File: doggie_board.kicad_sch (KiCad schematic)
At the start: 1 part, among them J2 Conn_01x02_Pin

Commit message: Cleaned up repo, fixing naming
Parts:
- removed J2: Conn_01x02_Pin, symbol Connector:Conn_01x02_Pin
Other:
- sheet Buck_Converter renamed 12v Buck Converter
- sheet Buck_Converter_2 renamed 5v Buck Converter
- sheet power_switch renamed High Side Power Switch
- removed sheet Buck_Converter3(Linear)
- sheet 12v Buck Converter: file untitled.kicad_sch -> buck12v.kicad_sch
- sheet 5v Buck Converter: file buckconv2.kicad_sch -> buck5v.kicad_sch
- company: (none) -> UMass Robotics 
- title: (none) -> UMR Power Board

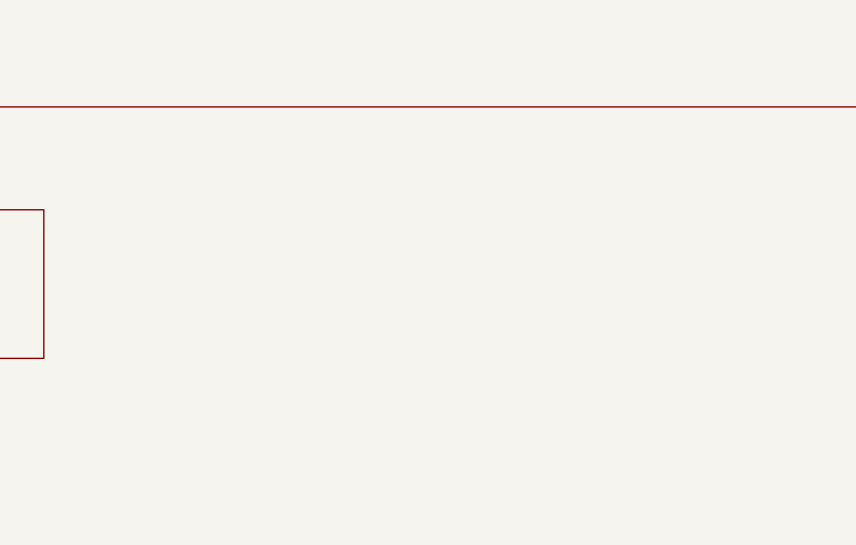
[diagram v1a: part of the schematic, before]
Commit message: moved schematics back to root folder
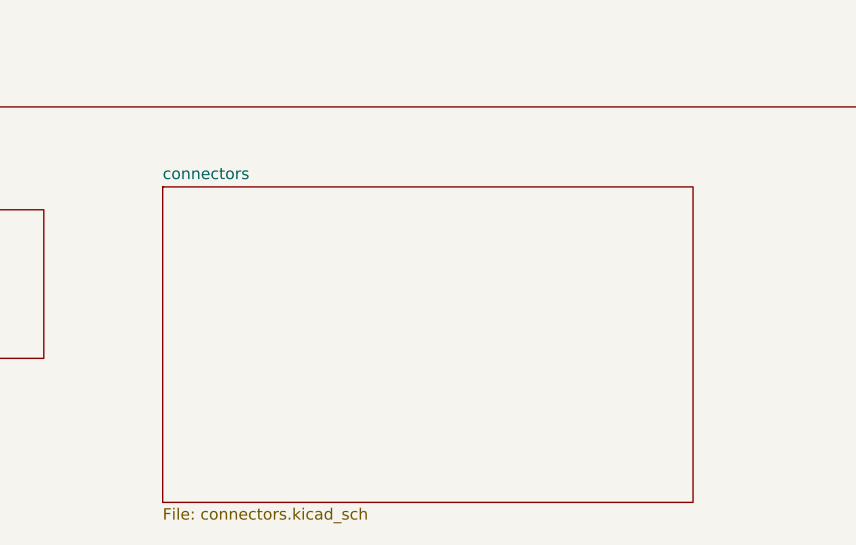
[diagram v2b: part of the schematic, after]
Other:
- added sheet connectors (connectors.kicad_sch)
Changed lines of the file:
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@@
+		)
+	)
+	(sheet
+		(at 70.358 113.03)
+		(size 58.928 35.052)
+		(exclude_from_sim no)
+		(in_bom yes)
+		(on_board yes)
+		(dnp no)
+		(fields_autoplaced yes)
+		(stroke
+			(width 0.1524)
+			(type solid)
+		)
+		(fill
+			(color 0 0 0 0.0000)
+		)
+		(property "Sheetname" "connectors"
+			(at 70.358 112.3184 0)
+			(effects
+				(font
+					(size 1.27 1.27)
+				)
+				(justify left bottom)
+			)
+		)
+		(property "Sheetfile" "connectors.kicad_sch"
+			(at 70.358 148.6666 0)
+			(effects
+				(font
+					(size 1.27 1.27)
+				)
+				(justify left top)
+			)
+		)
+		(instances
+			(project "doggie_board"
+				(path "/883cb7fa-3eb5-48d4-9cde-7c11307d94f0"
+					(page "5")
+				)
+			)
 		)
 	)

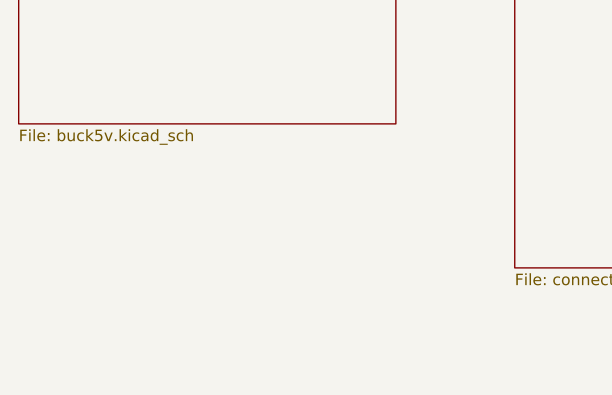
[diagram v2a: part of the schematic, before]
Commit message: 3.3v linear converter
added linear converter
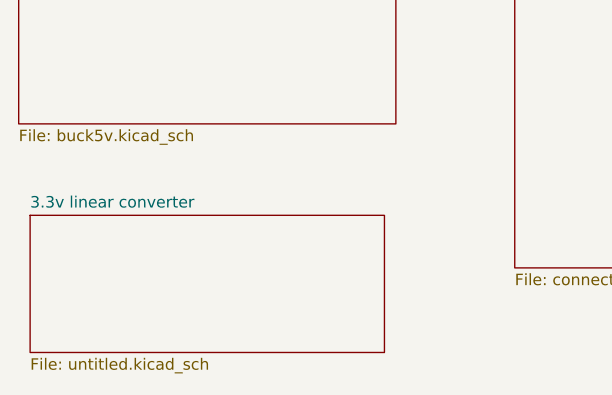
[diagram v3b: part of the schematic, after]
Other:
- added sheet 3.3v linear converter (untitled.kicad_sch)
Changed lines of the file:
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@@
+	)
+	(sheet
+		(at 16.51 142.24)
+		(size 39.37 15.24)
+		(exclude_from_sim no)
+		(in_bom yes)
+		(on_board yes)
+		(dnp no)
+		(fields_autoplaced yes)
+		(stroke
+			(width 0.1524)
+			(type solid)
+		)
+		(fill
+			(color 0 0 0 0.0000)
+		)
+		(property "Sheetname" "3.3v linear converter"
+			(at 16.51 141.5284 0)
+			(effects
+				(font
+					(size 1.27 1.27)
+				)
+				(justify left bottom)
+			)
+		)
+		(property "Sheetfile" "untitled.kicad_sch"
+			(at 16.51 158.0646 0)
+			(effects
+				(font
+					(size 1.27 1.27)
+				)
+				(justify left top)
+			)
+		)
+		(instances
+			(project "doggie_board"
+				(path "/883cb7fa-3eb5-48d4-9cde-7c11307d94f0"
+					(page "6")
+				)
+			)
+		)
 	)
 	(sheet

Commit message: Fixed Schematics with more cost effective IC's
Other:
- sheet 3.3v linear converter renamed 3.3v Buck Converter
- added sheet misc (misc.kicad_sch)
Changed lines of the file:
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@@
 			(color 0 0 0 0.0000)
 		)
-		(property "Sheetname" "3.3v linear converter"
+		(property "Sheetname" "3.3v Buck Converter"
 			(at 16.51 141.5284 0)
 			(effects
@@
 			(project "doggie_board"
 				(path "/883cb7fa-3eb5-48d4-9cde-7c11307d94f0"
-					(page "6")
+					(page "5")
 				)
 			)
@@
 	)
 	(sheet
+		(at 144.272 121.158)
+		(size 38.1 23.876)
+		(exclude_from_sim no)
+		(in_bom yes)
+		(on_board yes)
+		(dnp no)
+		(fields_autoplaced yes)
+		(stroke
+			(width 0.1524)
+			(type solid)
+		)
+		(fill
+			(color 0 0 0 0.0000)
+		)
+		(property "Sheetname" "misc"
+			(at 144.272 120.4464 0)
+			(effects
+				(font
+					(size 1.27 1.27)
+				)
+				(justify left bottom)
+			)
+		)
+		(property "Sheetfile" "misc.kicad_sch"
+			(at 144.272 145.6186 0)
+			(effects
+				(font
+					(size 1.27 1.27)
+				)
+				(justify left top)
+			)
+		)
+		(instances
+			(project "doggie_board"
+				(path "/883cb7fa-3eb5-48d4-9cde-7c11307d94f0"
+					(page "7")
+				)
+			)
+		)
+	)
+	(sheet
 		(at 70.358 113.03)
 		(size 58.928 35.052)
@@
 			(project "doggie_board"
 				(path "/883cb7fa-3eb5-48d4-9cde-7c11307d94f0"
-					(page "5")
+					(page "6")
 				)
 			)
